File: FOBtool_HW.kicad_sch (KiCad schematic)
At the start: 0 parts

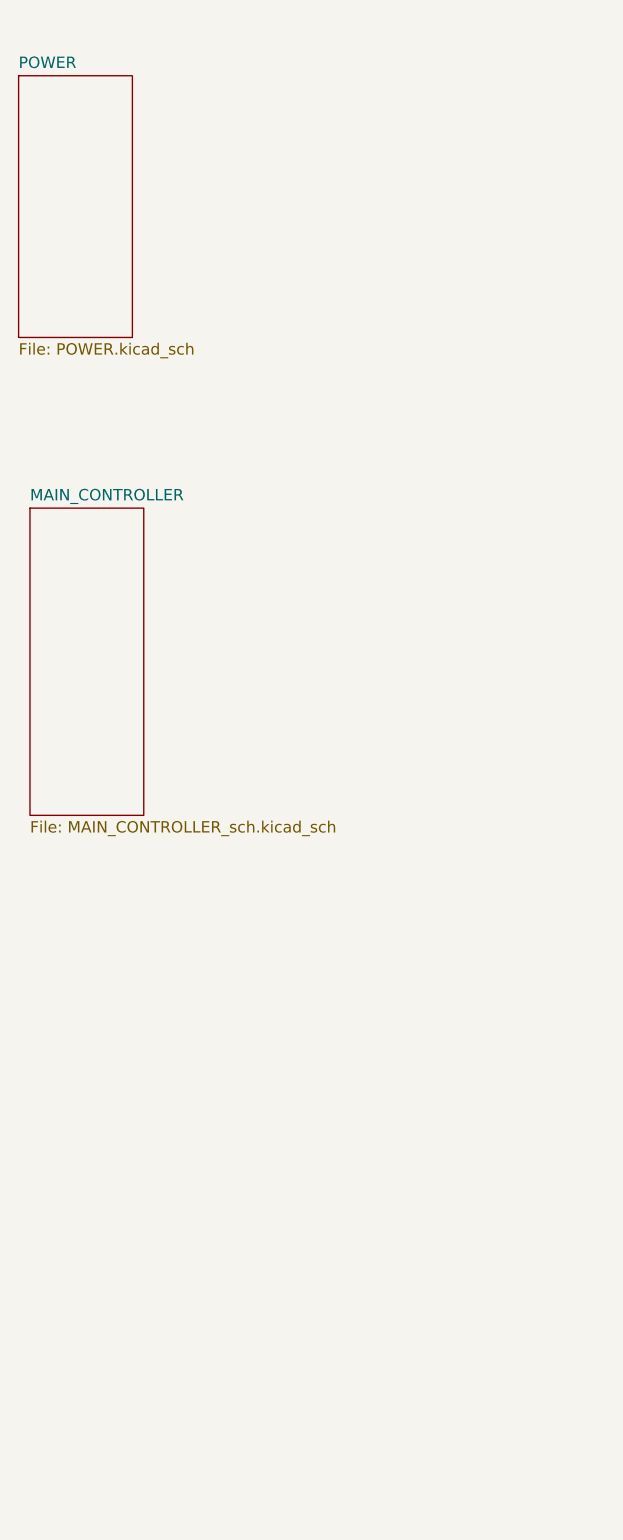
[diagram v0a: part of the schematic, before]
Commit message: finished SUB_GHZ_RF and RP2350 sheets however still the alue of tuning will be done after simulation
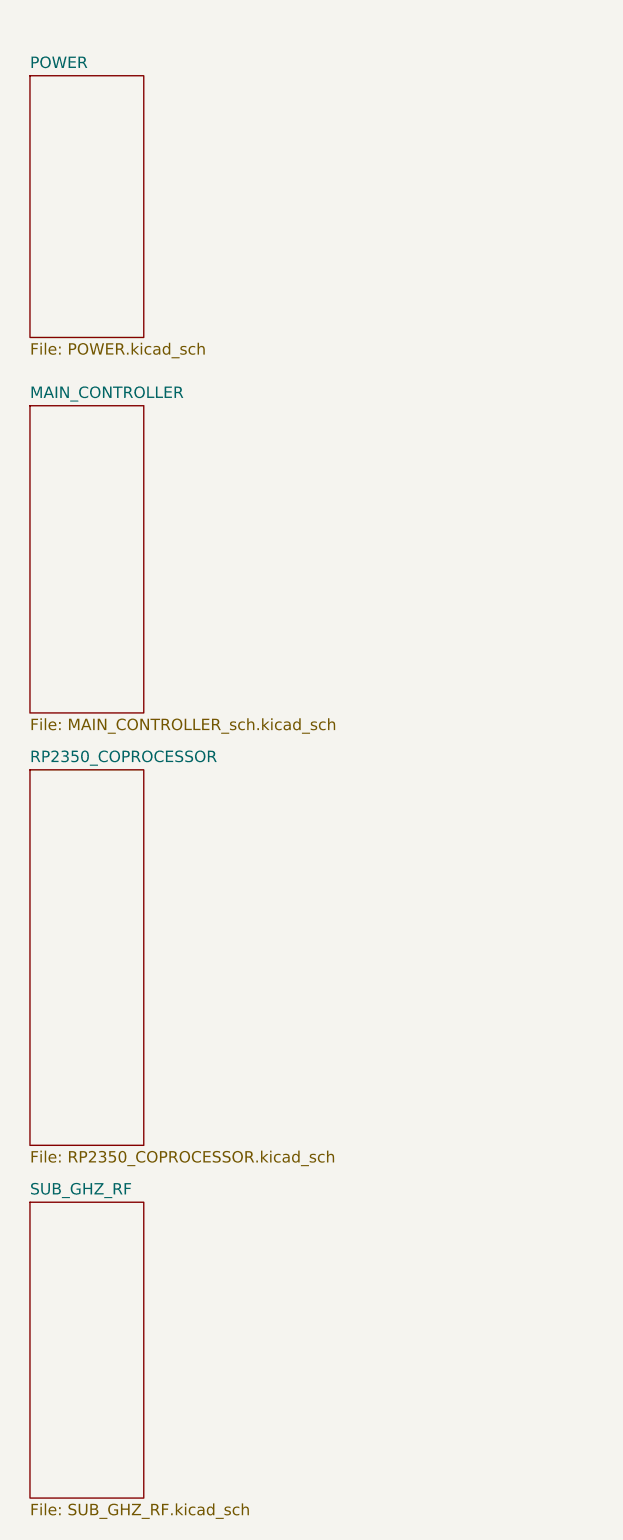
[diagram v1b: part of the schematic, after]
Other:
- added sheet RP2350_COPROCESSOR (RP2350_COPROCESSOR.kicad_sch)
- added sheet SUB_GHZ_RF (SUB_GHZ_RF.kicad_sch)
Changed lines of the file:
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@@
 	)
 	(sheet
-		(at 19.05 19.05)
+		(at 20.32 96.52)
+		(size 12.7 41.91)
+		(exclude_from_sim no)
+		(in_bom yes)
+		(on_board yes)
+		(dnp no)
+		(fields_autoplaced yes)
+		(stroke
+			(width 0.1524)
+			(type solid)
+		)
+		(fill
+			(color 0 0 0 0)
+		)
+		(property "Sheetname" "RP2350_COPROCESSOR"
+			(at 20.32 95.8084 0)
+			(show_name no)
+			(do_not_autoplace no)
+			(effects
+				(font
+					(size 1.27 1.27)
+				)
+				(justify left bottom)
+			)
+		)
+		(property "Sheetfile" "RP2350_COPROCESSOR.kicad_sch"
+			(at 20.32 139.0146 0)
+			(show_name no)
+			(do_not_autoplace no)
+			(effects
+				(font
+					(size 1.27 1.27)
+				)
+				(justify left top)
+			)
+		)
+		(instances
+			(project "FOBtool_HW"
+				(path "/4178b7d0-cf29-4cf2-b214-acbbbd97d338"
+					(page "4")
+				)
+			)
+		)
+	)
+	(sheet
+		(at 20.32 19.05)
 		(size 12.7 29.21)
 		(exclude_from_sim no)
@@
 		)
 		(property "Sheetname" "POWER"
-			(at 19.05 18.3384 0)
+			(at 20.32 18.3384 0)
 			(show_name no)
 			(do_not_autoplace no)
@@
 		)
 		(property "Sheetfile" "POWER.kicad_sch"
-			(at 19.05 48.8446 0)
+			(at 20.32 48.8446 0)
 			(show_name no)
 			(do_not_autoplace no)
@@
 	)
 	(sheet
-		(at 20.32 67.31)
+		(at 20.32 144.78)
+		(size 12.7 33.02)
+		(exclude_from_sim no)
+		(in_bom yes)
+		(on_board yes)
+		(dnp no)
+		(fields_autoplaced yes)
+		(stroke
+			(width 0.1524)
+			(type solid)
+		)
+		(fill
+			(color 0 0 0 0)
+		)
+		(property "Sheetname" "SUB_GHZ_RF"
+			(at 20.32 144.0684 0)
+			(show_name no)
+			(do_not_autoplace no)
+			(effects
+				(font
+					(size 1.27 1.27)
+				)
+				(justify left bottom)
+			)
+		)
+		(property "Sheetfile" "SUB_GHZ_RF.kicad_sch"
+			(at 20.32 178.3846 0)
+			(show_name no)
+			(do_not_autoplace no)
+			(effects
+				(font
+					(size 1.27 1.27)
+				)
+				(justify left top)
+			)
+		)
+		(instances
+			(project "FOBtool_HW"
+				(path "/4178b7d0-cf29-4cf2-b214-acbbbd97d338"
+					(page "5")
+				)
+			)
+		)
+	)
+	(sheet
+		(at 20.32 55.88)
 		(size 12.7 34.29)
 		(exclude_from_sim no)
@@
 		)
 		(property "Sheetname" "MAIN_CONTROLLER"
-			(at 20.32 66.5984 0)
+			(at 20.32 55.1684 0)
 			(show_name no)
 			(do_not_autoplace no)
@@
 		)
 		(property "Sheetfile" "MAIN_CONTROLLER_sch.kicad_sch"
-			(at 20.32 102.1846 0)
+			(at 20.32 90.7546 0)
 			(show_name no)
 			(do_not_autoplace no)

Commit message: Finished Last sheets
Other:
- added sheet HMI (HMI.kicad_sch)
- added sheet POSITIONING (POSITIONING.kicad_sch)
- added sheet WIRED_IO (WIRED_IO.kicad_sch)
- sheet MAIN_CONTROLLER ports: added BUZZER, CONSOLE_RX, CONSOLE_TX, ENCODER_A, ENCODER_B, ENCODER_SW, ESP_BOOT, ESP_EN, GPS_PPS, GPS_RX, GPS_TX, HAPTIC_TRIG, I2C_SCL, I2C_SDA, LINK_ESP_RX, LINK_ESP_TX, LINK_SYNC, RF_SW_A, SPI_MISO, SPI_MOSI, SPI_SCK, TFT_BL_PWM, TFT_DC, TFT_RST, UWB_IRQ, UWB_RST, WS2812_DATA, ZEROIZE_BTN, nCS_CC1101_A, nCS_CC1101_B, nCS_CC1101_C, nCS_SD, nCS_SI4463, nCS_TFT, nCS_UWB; removed none
- sheet POWER ports: added BOOST_5V_EN, CHG_CE_N, CHG_USB_DM, CHG_USB_DP, I2C_SCL, I2C_SDA, USB_HOST_FAULT_N, USB_HOST_VBUS_EN, USB_MUX_SEL, VBUS_HOST; removed none
- sheet RP2350_COPROCESSOR ports: added CAN_RX, CAN_STBY, CAN_TX, CC1101_A_GDO0, CC1101_B_GDO0, CC1101_C_GDO0, LF_COIL_SEL, LF_SCIO, LF_TXCT, LINK_ESP_RX, LINK_ESP_TX, LINK_SYNC, NFC_IRQ, NFC_MISO, NFC_MOSI, NFC_SCK, REPLAY_OUT, USBC_CC1_SENSE, USBC_CC2_SENSE, USB_HOST_D_N, USB_HOST_D_P, USB_HOST_FAULT_N, USB_HOST_VBUS_EN, nCS_NFC; removed none
- sheet SUB_GHZ_RF ports: added BOOST_5V_EN, CC1101_A_GDO0, CC1101_B_GDO0, CC1101_C_GDO0, CHG_CE_N, I2C_SCL, I2C_SDA, REPLAY_OUT, RF_SW_A, SPI_MISO, SPI_MOSI, SPI_SCK, nCS_CC1101_A, nCS_CC1101_B, nCS_CC1101_C, nCS_SI4463; removed none

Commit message: finished annotation
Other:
- sheet POWER ports: added none; removed CHG_USB_DM, CHG_USB_DP, USB_MUX_SEL
- sheet RP2350_COPROCESSOR ports: added NFC_DWL_REQ, NFC_VEN; removed none
- note added: "Notes Power: Keep CHG_CE_N high, BOOST_5V_EN low and USB_HOST_VBUS_EN low during initialization. Set charger input-current limit from the detected USB-C source. Enable +5V_SYS before VBUS_HOST and reverse the sequence during shutdown. RP2350/WIRED_IO: Default USB_HOST_VBUS_EN low. Monitor USB_HOST_FAULT_N and immediately disable VBUS_HOST on an asserted fault. HMI: TCA9534 address = 0x21. Configu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"
- note removed: "POWER-SHEET CRITICAL NOTES BATTERY: Use only a protected 1S Li-ion battery pack. Verify connector keying and polarity before assembly or power application. REV-A LIMITATION: The 2-wire battery pack provides no thermistor connection. TS is fixed-biased and does not provide actual battery-temperature monitoring. FIRMWARE: At every charger initialization, program BQ25895 REG04 ICHG to 1.024 A and ve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"
- title: (none) -> FOBtool Handheld RF Security Platform

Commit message: finished ANCHOR_DOCK sheet
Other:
- added sheet ANCHOR_DOCK (untitled.kicad_sch)
- sheet RP2350_COPROCESSOR ports: added DOCK_FAULT_N, DOCK_LINK_A, DOCK_LINK_B, DOCK_SENSE, DOCK_SYNC, DOCK_VBUS_EN; removed none

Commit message: the schematic is finished
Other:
- sheet ANCHOR_DOCK: file untitled.kicad_sch -> ANCHOR_DOCK.kicad_sch
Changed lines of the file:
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@@
-			)
-		)
-		(pin "DOCK_LINK_A" input
-			(at 78.74 138.43 0)
-			(effects
-				(font
-					(size 1.27 1.27)
-				)
-				(justify right)
 			)
 		)
@@
 		(pin "DOCK_VBUS_EN" output
 			(at 78.74 148.59 0)
+			(effects
+				(font
+					(size 1.27 1.27)
+				)
+				(justify right)
+			)
+		)
+		(pin "DOCK_LINK_A" output
+			(at 78.74 138.43 0)
 			(effects
 				(font
@@
 			)
 		)
-		(property "Sheetfile" "untitled.kicad_sch"
+		(property "Sheetfile" "ANCHOR_DOCK.kicad_sch"
 			(at 62.23 180.9246 0)
 			(show_name no)

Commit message: first revision before changing spi
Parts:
- added H1, H2, H3, H4: MountingHole, MountingHole:MountingHole_2.2mm_M2, symbol Mechanical:MountingHole
